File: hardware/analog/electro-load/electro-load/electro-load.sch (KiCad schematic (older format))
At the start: 10 parts

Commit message: Added datasheets for noctua fan, mcu and lm358 etc.
Finished schematic rev 1 of electro load
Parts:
- removed J? (x2): Conn_01x01_Female, symbol Connector:Conn_01x01_Female
- removed R?: R_Small, symbol Device:R_Small
- removed RV?: R_POT, symbol Device:R_POT
- removed U?: OPAMP, symbol pspice:OPAMP
- removed U?: ATMEGA328P-AU, digikey-footprints:TQFP-32_7x7mm, symbol dk_Embedded-Microcontrollers:ATMEGA328P-AU
- added C1, C4, C5, C7: 10u, Capacitor_SMD:C_0603_1608Metric, symbol Device:C_Small
- added C2, C3, C6: 100n, Capacitor_SMD:C_0603_1608Metric, symbol Device:C_Small
- added D1: STATUS, LED_THT:LED_D5.0mm-4_RGB_Wide_Pins, symbol Device:LED_ABRG
- added D3: D_Schottky, athir:SOD80C(Reflow), symbol Device:D_Schottky
- added J1: Barrel_Jack, athir:6778759, symbol Connector:Barrel_Jack
- added J3: AVR-ISP-10, Connector_PinHeader_2.54mm:PinHeader_2x05_P2.54mm_Vertical, symbol Connector:AVR-ISP-10
- added K1: SANYOU_SRD_Form_C, Relay_THT:Relay_SPDT_SANYOU_SRD_Series_Form_C, symbol Relay:SANYOU_SRD_Form_C
- added M1: Noctua NF-A14 5V, Connector_PinHeader_2.54mm:PinHeader_1x04_P2.54mm_Vertical, symbol Motor:Fan_4pin
- added Q2, Q4: 2N2222A, Package_TO_SOT_THT:TO-92_Inline, symbol dk_Transistors-Bipolar-BJT-Single:2N2222A
- added Q3: 2N2222, Package_TO_SOT_THT:TO-92_Inline, symbol dk_Transistors-Bipolar-BJT-Single:2N2222
- added R1: 2k, Resistor_SMD:R_0603_1608Metric, symbol Device:R_Small
- added R11: 825k, Resistor_SMD:R_0603_1608Metric, symbol Device:R_Small
- added R13: 2ohm 128++W, Connector_PinSocket_2.54mm:PinSocket_1x02_P2.54mm_Vertical, symbol Device:R_Small
- added R14, R15, R20, R21: 10k POT, Potentiometer_SMD:Potentiometer_Bourns_3214W_Vertical, symbol Device:R_Small
- added R16, R17, R22, R23, R24, R28, R29, R30: 1k, Resistor_SMD:R_0603_1608Metric, symbol Device:R_Small
- added R18, R4, R5: 4k7, Resistor_SMD:R_0603_1608Metric, symbol Device:R_Small
- added R19, R25: 3k3, Resistor_SMD:R_0603_1608Metric, symbol Device:R_Small
- added R2: 220, Resistor_SMD:R_0603_1608Metric, symbol Device:R_Small
- added R26, R27, R3: 10k, Resistor_SMD:R_0603_1608Metric, symbol Device:R_Small
- added R6: 200, Resistor_SMD:R_0603_1608Metric, symbol Device:R_Small
- added R8: 10M 1%, Resistor_SMD:R_0603_1608Metric, symbol Device:R_Small
- added R9: 1M5 1%, Resistor_SMD:R_0603_1608Metric, symbol Device:R_Small
- added SW1: RESET, symbol Switch:SW_Push
- added TP1, TP10, TP11, TP12, TP13, TP2, TP3, TP4, TP5, TP6, TP7, TP8, TP9: TestPoint, athir:testpoint_probe, symbol Connector:TestPoint
- added U2: ATmega328P-AU, Package_QFP:TQFP-32_7x7mm_P0.8mm, symbol MCU_Microchip_ATmega:ATmega328P-AU
- added U3: MCP4725A0T-E_CH, digikey-footprints:SOT-23-6, symbol dk_Data-Acquisition-Digital-to-Analog-Converters-DAC:MCP4725A0T-E_CH
- added U4, U5: LM358DR, digikey-footprints:SOIC-8_W3.9mm, symbol dk_Linear-Amplifiers-Instrumentation-OP-Amps-Buffer-Amps:LM358DR
- Q1: renamed from Q?; footprint (none) -> Package_TO_SOT_SMD:TO-263-2
- R10: renamed from R?; value R_Small -> 2M; footprint (none) -> Resistor_SMD:R_0603_1608Metric
- R12: renamed from R?; value 2ohm -> 2R 128++W; footprint (none) -> Connector_PinSocket_2.54mm:PinSocket_1x02_P2.54mm_Vertical
- gave numbers to parts that had none: 1
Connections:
- net labels added: CUR_MEAS, CUR_SET, FAN_PWM, FAN_RPM, LCD_DB4, LCD_DB5, LCD_DB6, LCD_DB7, LCD_EN, LCD_RS, LCD_RW, MISO, MOSI, RELAY_EN, SCK, SCL, SDA, STATUS_B, STATUS_G, STATUS_R, TEMP_0, TEMP_1, VCC, V_IN, ~RESET
- wire segments 19 -> 227
- no-connect marks 0 -> 12
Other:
- note added: "DC_OFFSET\nZERO OFFSET"
- note added: "GAIN"
- note added: "OBS: 2N2222A vs -A har forskelligt PINOUT!!"
- moved on the sheet: R10, R12, U1

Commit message: Spread schematic out into multiple subsheets. Removed LEDs as pins was needed for 16x2 display
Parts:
- removed D1: STATUS, LED_THT:LED_D5.0mm-4_RGB_Wide_Pins, symbol Device:LED_ABRG
- removed D3: D_Schottky, athir:SOD80C(Reflow), symbol Device:D_Schottky
- removed J1: Barrel_Jack, athir:6778759, symbol Connector:Barrel_Jack
- removed K1: SANYOU_SRD_Form_C, Relay_THT:Relay_SPDT_SANYOU_SRD_Series_Form_C, symbol Relay:SANYOU_SRD_Form_C
- removed M1: Noctua NF-A14 5V, Connector_PinHeader_2.54mm:PinHeader_1x04_P2.54mm_Vertical, symbol Motor:Fan_4pin
- removed Q1: Q_NJFET_GDS, Package_TO_SOT_SMD:TO-263-2, symbol Device:Q_NJFET_GDS
- removed Q2, Q4: 2N2222A, Package_TO_SOT_THT:TO-92_Inline, symbol dk_Transistors-Bipolar-BJT-Single:2N2222A
- removed Q3: 2N2222, Package_TO_SOT_THT:TO-92_Inline, symbol dk_Transistors-Bipolar-BJT-Single:2N2222
- removed R1: 2k, Resistor_SMD:R_0603_1608Metric, symbol Device:R_Small
- removed R10: 2M, Resistor_SMD:R_0603_1608Metric, symbol Device:R_Small
- removed R11: 825k, Resistor_SMD:R_0603_1608Metric, symbol Device:R_Small
- removed R12: 2R 128++W, Connector_PinSocket_2.54mm:PinSocket_1x02_P2.54mm_Vertical, symbol Device:R_Small
- removed R13: 2ohm 128++W, Connector_PinSocket_2.54mm:PinSocket_1x02_P2.54mm_Vertical, symbol Device:R_Small
- removed R14, R15, R20, R21: 10k POT, Potentiometer_SMD:Potentiometer_Bourns_3214W_Vertical, symbol Device:R_Small
- removed R16, R17, R22, R23, R24, R28, R29, R30: 1k, Resistor_SMD:R_0603_1608Metric, symbol Device:R_Small
- removed R18: 4k7, Resistor_SMD:R_0603_1608Metric, symbol Device:R_Small
- removed R19, R25: 3k3, Resistor_SMD:R_0603_1608Metric, symbol Device:R_Small
- removed R2: 220, Resistor_SMD:R_0603_1608Metric, symbol Device:R_Small
- removed R26, R27: 10k, Resistor_SMD:R_0603_1608Metric, symbol Device:R_Small
- removed R6: 200, Resistor_SMD:R_0603_1608Metric, symbol Device:R_Small
- removed R8: 10M 1%, Resistor_SMD:R_0603_1608Metric, symbol Device:R_Small
- removed R9: 1M5 1%, Resistor_SMD:R_0603_1608Metric, symbol Device:R_Small
- removed TP10, TP11, TP12, TP13, TP4, TP5, TP6, TP7, TP8, TP9: TestPoint, athir:testpoint_probe, symbol Connector:TestPoint
- removed U1: RC1602A, Displays:RC1602A, symbol athir:RC1602A
- removed U4, U5: LM358DR, digikey-footprints:SOIC-8_W3.9mm, symbol dk_Linear-Amplifiers-Instrumentation-OP-Amps-Buffer-Amps:LM358DR
- renumbered J3 to J1, R3 to R1, R4 to R2, R5 to R3, U2 to U1, U3 to U2
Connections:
- net labels removed: VCC, V_IN
- wire segments 227 -> 65
- no-connect marks 12 -> 3
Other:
- note removed: "DC_OFFSET\nZERO OFFSET"
- note removed: "GAIN"
- note removed: "OBS: 2N2222A vs -A har forskelligt PINOUT!!"

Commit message: HW rev 1 of electronic load PCB.
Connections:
- net LCD_DB5: now also U1.11 (PD7); no longer U1.9 (PD5)
- net LCD_DB7: now also U1.9 (PD5); no longer U1.11 (PD7)
- net V_MEAS: now reaches U1.24 (PC1)
- net STATUS_B renamed ROT_SW
- net STATUS_G renamed ROT_B
- net STATUS_R renamed ROT_A
- no-connect marks 3 -> 2
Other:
- note added: "OBS"
- moved on the sheet: J1
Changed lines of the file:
@@
 EESchema Schematic File Version 4
-LIBS:electro-load-cache
 EELAYER 30 0
 EELAYER END
@@
 Wire Wire Line
 	2000 7025 2000 6975
-Text Label 2600 4875 0    50   ~ 0
-STATUS_R
-Text Label 2600 4975 0    50   ~ 0
-STATUS_G
-Text Label 2600 5975 0    50   ~ 0
-STATUS_B
-Wire Wire Line
-	2875 5175 2600 5175
 Text Label 2600 4475 0    50   ~ 0
 RELAY_EN
@@
 Text Label 2600 5375 0    50   ~ 0
 TEMP_1
-Text Label 2875 5175 0    50   ~ 0
+Text Label 2600 5175 0    50   ~ 0
 CUR_MEAS
 Text Label 4425 1875 0    50   ~ 0
@@
 Wire Wire Line
 	2600 4000 2400 4000
-Text Label 10975 5675 0    50   ~ 0
+Text Label 8750 5500 0    50   ~ 0
 MOSI
-Text Label 10975 5875 0    50   ~ 0
+Text Label 8750 5700 0    50   ~ 0
 ~RESET
-Text Label 10975 5775 0    50   ~ 0
+Text Label 8750 5600 0    50   ~ 0
 SCK
-Text Label 10975 5575 0    50   ~ 0
+Text Label 8750 5400 0    50   ~ 0
 MISO
 $Comp
 L power:+5V #PWR012
 U 1 1 5E81DCEE
-P 10475 5225
-F 0 "#PWR012" H 10475 5075 50  0001 C CNN
-F 1 "+5V" H 10490 5398 50  0000 C CNN
-F 2 "" H 10475 5225 50  0001 C CNN
-F 3 "" H 10475 5225 50  0001 C CNN
-	1    10475 5225
+P 8250 5050
+F 0 "#PWR012" H 8250 4900 50  0001 C CNN
+F 1 "+5V" H 8265 5223 50  0000 C CNN
+F 2 "" H 8250 5050 50  0001 C CNN
+F 3 "" H 8250 5050 50  0001 C CNN
+	1    8250 5050
 	1    0    0    -1
 $EndComp
@@
 L power:GND #PWR013
 U 1 1 5E8275B7
-P 10475 6250
-F 0 "#PWR013" H 10475 6000 50  0001 C CNN
-F 1 "GND" H 10480 6077 50  0000 C CNN
-F 2 "" H 10475 6250 50  0001 C CNN
-F 3 "" H 10475 6250 50  0001 C CNN
-	1    10475 6250
+P 8250 6075
+F 0 "#PWR013" H 8250 5825 50  0001 C CNN
+F 1 "GND" H 8255 5902 50  0000 C CNN
+F 2 "" H 8250 6075 50  0001 C CNN
+F 3 "" H 8250 6075 50  0001 C CNN
+	1    8250 6075
 	1    0    0    -1
 $EndComp
@@
 L Connector:AVR-ISP-10 J1
 U 1 1 5E855F65
-P 10575 5775
-F 0 "J1" H 10295 5871 50  0000 R CNN
-F 1 "AVR-ISP-10" H 10295 5780 50  0000 R CNN
-F 2 "Connector_PinHeader_2.54mm:PinHeader_2x05_P2.54mm_Vertical" V 10325 5825 50  0001 C CNN
-F 3 " ~" H 9300 5225 50  0001 C CNN
-	1    10575 5775
-	1    0    0    -1
-$EndComp
-Wire Wire Line
-	10475 6250 10475 6175
-Wire Wire Line
-	10475 5225 10475 5275
+P 8350 5600
+F 0 "J1" H 8070 5696 50  0000 R CNN
+F 1 "AVR-ISP-10" H 8070 5605 50  0000 R CNN
+F 2 "Connector_PinHeader_2.54mm:PinHeader_2x05_P2.54mm_Vertical" V 8100 5650 50  0001 C CNN
+F 3 " ~" H 7075 5050 50  0001 C CNN
+	1    8350 5600
+	1    0    0    -1
+$EndComp
+Wire Wire Line
+	8250 6075 8250 6000
+Wire Wire Line
+	8250 5050 8250 5100
 Text Label 2600 4575 0    50   ~ 0
 MOSI
@@
 Connection ~ 3975 1250
 $Sheet
-S 4850 6900 700  525
+S 4650 6100 700  525
 U 5E8D69C1
 F0 "Power" 50
@@
 Text Label 2600 6075 0    50   ~ 0
 LCD_EN
-Text Label 2600 6675 0    50   ~ 0
+Text Label 2600 6475 0    50   ~ 0
 LCD_DB7
 Text Label 2600 6575 0    50   ~ 0
 LCD_DB6
-Text Label 2600 6475 0    50   ~ 0
+Text Label 2600 6675 0    50   ~ 0
 LCD_DB5
 Text Label 2600 6375 0    50   ~ 0
 LCD_DB4
-NoConn ~ 2600 5275
 $Sheet
-S 3825 6800 675  525
+S 5200 4125 1025 200
 U 5E789C0B
 F0 "Temperature Control" 50
 F1 "tempctl.sch" 50
+F2 "TEMP_1" I L 5200 4250 50
+F3 "TEMP_0" I L 5200 4175 50
+F4 "FAN_RPM" I R 6225 4175 50
+F5 "FAN_PWM" I R 6225 4250 50
 $EndSheet
 $Sheet
-S 5725 6425 1050 1000
+S 5300 5000 875  575
 U 5E7EC7EF
 F0 "UI" 50
 F1 "ui.sch" 50
+F2 "LCD_RS" I L 5300 5050 50
+F3 "LCD_RW" I L 5300 5125 50
+F4 "LCD_EN" I L 5300 5200 50
+F5 "LCD_DB4" I L 5300 5275 50
+F6 "LCD_DB5" I L 5300 5350 50
+F7 "LCD_DB6" I L 5300 5425 50
+F8 "LCD_DB7" I L 5300 5500 50
+F9 "ROT_SW" I R 6175 5050 50
+F10 "ROT_A" I R 6175 5125 50
+F11 "ROT_B" I R 6175 5200 50
 $EndSheet
 $Sheet
-S 6850 1950 1675 1625
+S 6850 1950 1075 275
 U 5E82E2D2
 F0 "Current Measurements" 50
 F1 "current.sch" 50
+F2 "V_MEAS" I R 7925 2025 50
+F3 "CUR_MEAS" I L 6850 2025 50
+F4 "CUR_SET" I L 6850 2125 50
+F5 "RELAY_EN" I R 7925 2125 50
 $EndSheet
+Text Label 5300 5050 2    50   ~ 0
+LCD_RS
+Text Label 5300 5125 2    50   ~ 0
+LCD_RW
+Text Label 5300 5200 2    50   ~ 0
+LCD_EN
+Text Label 5300 5500 2    50   ~ 0
+LCD_DB7
+Text Label 5300 5425 2    50   ~ 0
+LCD_DB6
+Text Label 5300 5350 2    50   ~ 0
+LCD_DB5
+Text Label 5300 5275 2    50   ~ 0
+LCD_DB4
+Text Label 5200 4250 2    50   ~ 0
+TEMP_1
+Text Label 5200 4175 2    50   ~ 0
+TEMP_0
+Text Label 6225 4250 0    50   ~ 0
+FAN_PWM
+Text Label 6225 4175 0    50   ~ 0
+FAN_RPM
+Text Label 7925 2125 0    50   ~ 0
+RELAY_EN
+Text Label 6850 2025 2    50   ~ 0
+CUR_MEAS
+Text Label 6850 2125 2    50   ~ 0
+CUR_SET
+Text Label 2600 5275 0    50   ~ 0
+V_MEAS
+Text Label 7925 2025 0    50   ~ 0
+V_MEAS
+Text Label 6175 5050 0    50   ~ 0
+ROT_SW
+Text Label 6175 5125 0    50   ~ 0
+ROT_A
+Text Label 6175 5200 0    50   ~ 0
+ROT_B
+Text Label 2600 5975 0    50   ~ 0
+ROT_SW
+Text Label 2600 4875 0    50   ~ 0
+ROT_A
+Text Label 2600 4975 0    50   ~ 0
+ROT_B
+Text Notes 3050 6525 0    50   ~ 0
+OBS
 $EndSCHEMATC

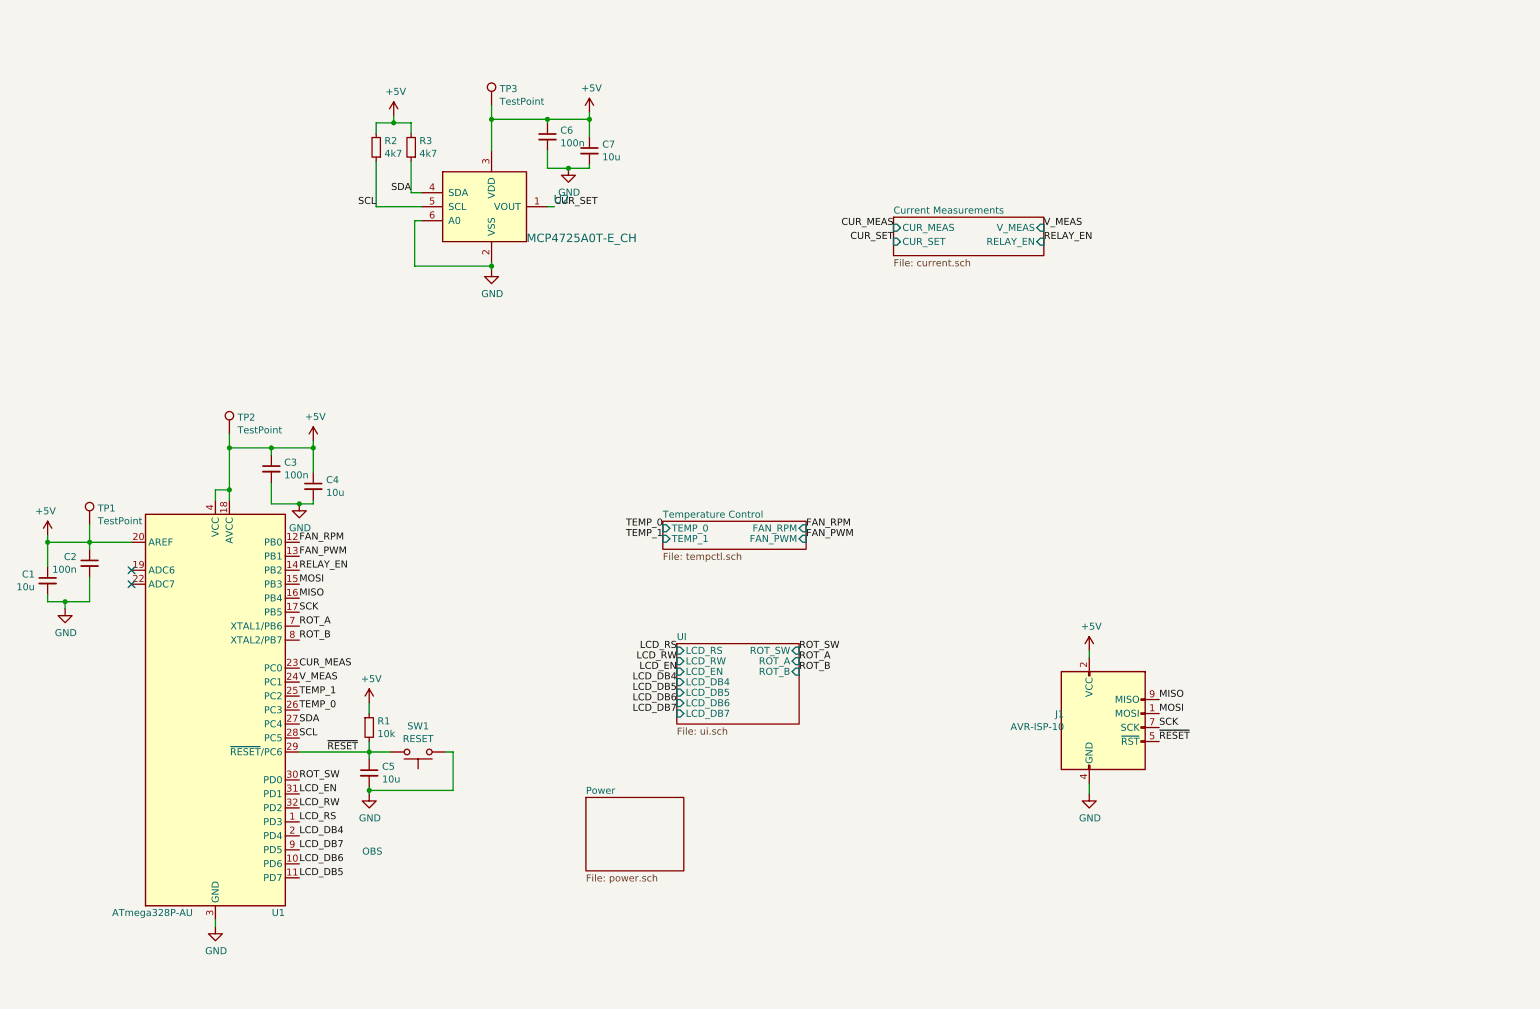
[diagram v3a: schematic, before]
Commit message: Added voltage reference REF5020 datasheet
Started work on HW rev 2 of electro load and 5v-from-mains - rev 1 contained misaligned footprints.
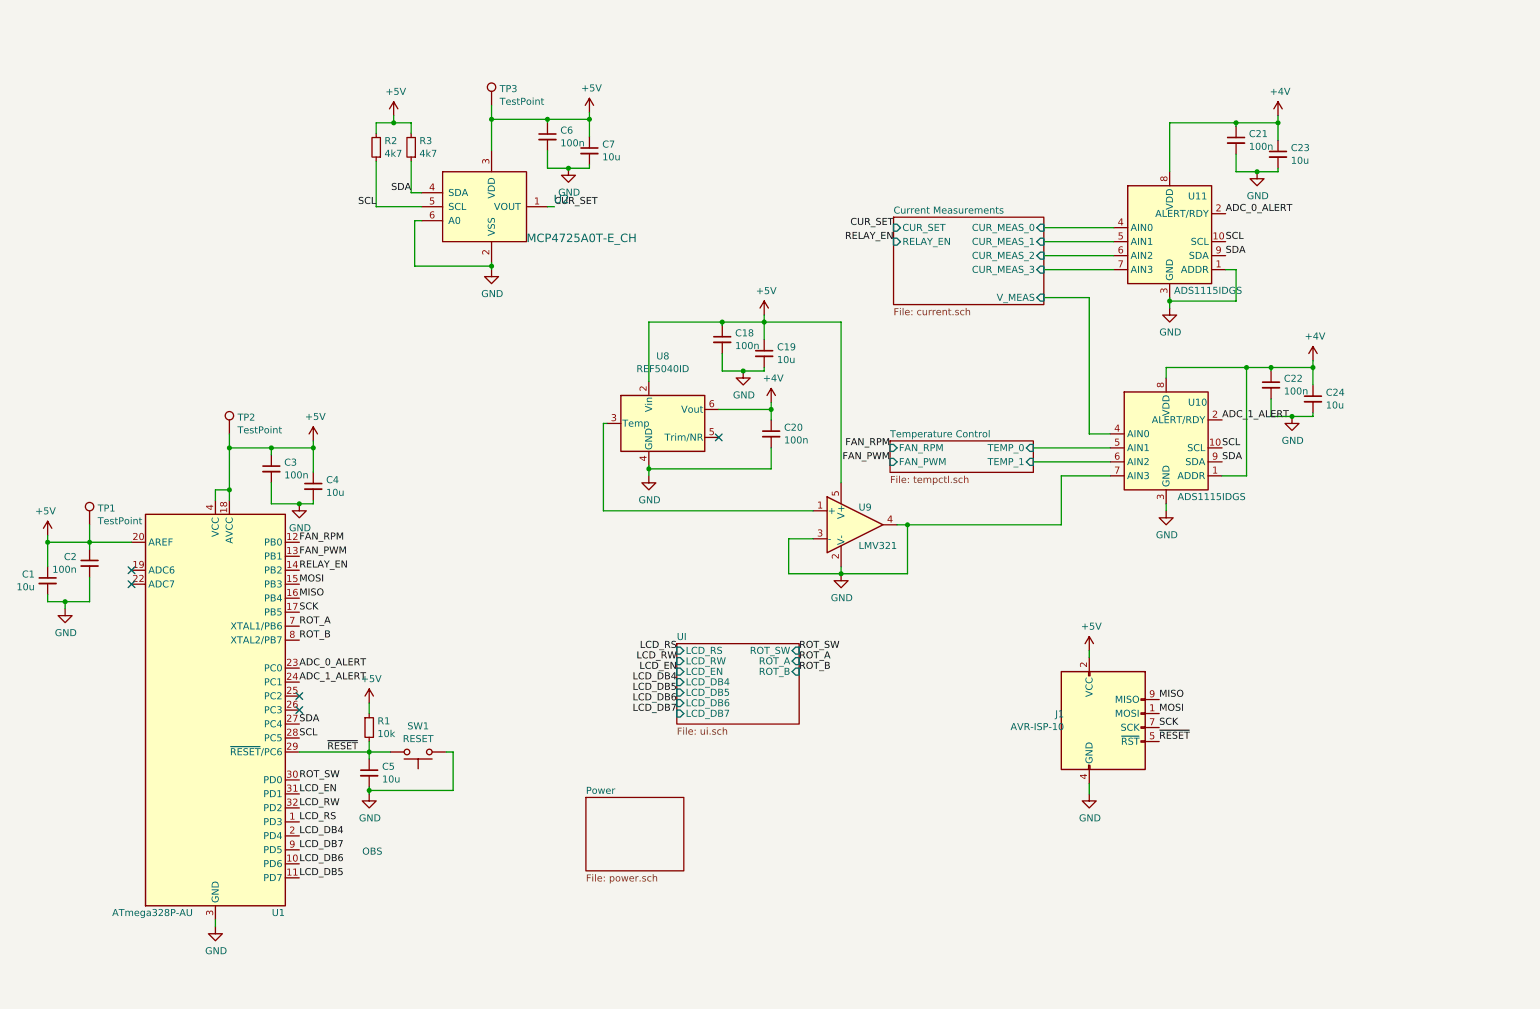
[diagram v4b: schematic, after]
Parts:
- added C18, C20, C21, C22: 100n, Capacitor_SMD:C_0603_1608Metric, symbol Device:C_Small
- added C19, C23, C24: 10u, Capacitor_SMD:C_0603_1608Metric, symbol Device:C_Small
- added U10, U11: ADS1115IDGS, Package_SO:TSSOP-10_3x3mm_P0.5mm, symbol Analog_ADC:ADS1115IDGS
- added U8: REF5040ID, Package_SO:SOIC-8_3.9x4.9mm_P1.27mm, symbol Reference_Voltage:REF5040ID
- added U9: LMV321, Package_TO_SOT_SMD:SOT-23-5, symbol Amplifier_Operational:LMV321
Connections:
- net +5V: now also C18.1, C19.1, U8.2 (Vin), U9.5 (V+)
- net GND: now also C18.2, C19.2, C20.2, C21.2, C22.2, C23.2, C24.2, U10.3 (GND), U10.7 (AIN3), U11.1 (ADDR), U11.3 (GND), U8.4 (GND), U9.2 (V-), U9.3 (-), U9.4
- net SCL: now also U10.10 (SCL), U11.10 (SCL)
- net SDA: now also U10.9 (SDA), U11.9 (SDA)
- net CUR_MEAS renamed ADC_0_ALERT
- net ADC_0_ALERT: now also U11.2 (ALERT/RDY)
- net TEMP_0: no longer names the net of U1.26 (PC3)
- net TEMP_1: no longer names the net of U1.25 (PC2)
- net V_MEAS renamed ADC_1_ALERT
- net ADC_1_ALERT: now also U10.2 (ALERT/RDY)
- new net: U8.3 (Temp), U9.1 (+)
- new net +4V: C20.1, C21.1, C22.1, C23.1, C24.1, U10.1 (ADDR), U10.8 (VDD), U11.8 (VDD), U8.6 (Vout)
- new net Current Measurements/CUR_MEAS_0: U11.4 (AIN0)
- new net Current Measurements/CUR_MEAS_1: U11.5 (AIN1)
- new net Current Measurements/CUR_MEAS_2: U11.6 (AIN2)
- new net Current Measurements/CUR_MEAS_3: U11.7 (AIN3)
- new net Current Measurements/V_MEAS: U10.4 (AIN0)
- new net Temperature Control/TEMP_0: U10.5 (AIN1)
- new net Temperature Control/TEMP_1: U10.6 (AIN2)
- no-connect marks 2 -> 5

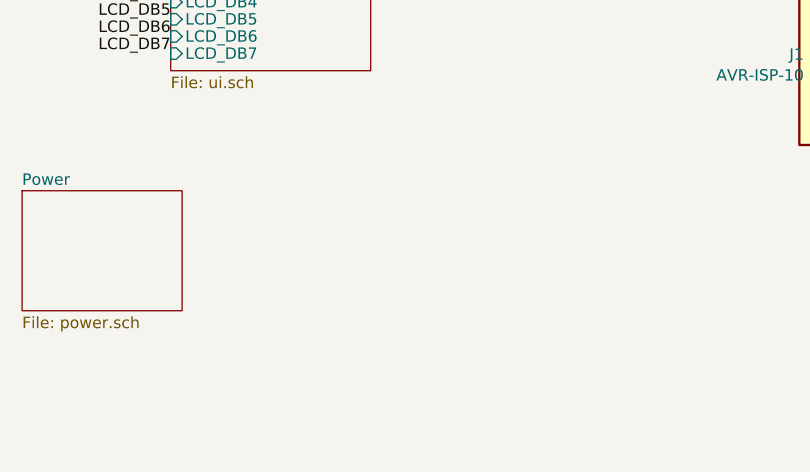
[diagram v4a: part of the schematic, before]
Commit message: Arranged mosfets and temperature probes to amplifier casing.
Added Power schematic from 5v-from-mains
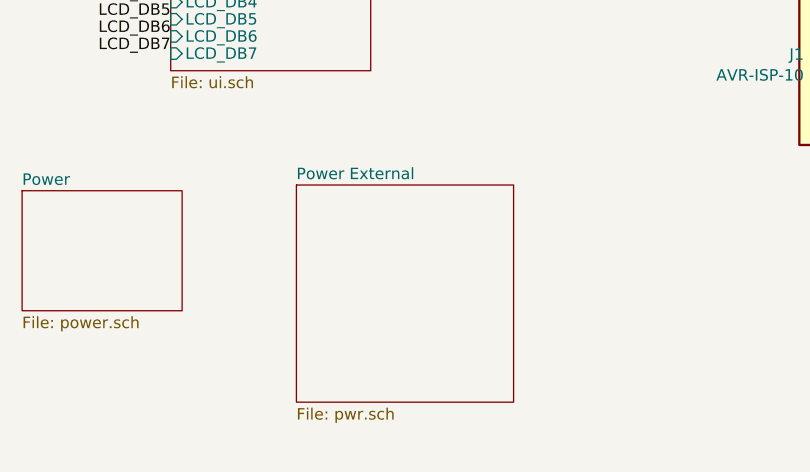
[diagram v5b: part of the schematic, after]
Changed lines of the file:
@@
 EESchema Schematic File Version 4
+LIBS:electro-load-cache
 EELAYER 30 0
 EELAYER END
 $Descr A4 11693 8268
 encoding utf-8
-Sheet 1 5
+Sheet 1 6
 Title ""
 Date ""
@@
 NoConn ~ 2600 5375
 NoConn ~ 2600 5475
+$Sheet
+S 5850 6075 950  950
+U 5E9F0954
+F0 "Power External" 50
+F1 "pwr.sch" 50
+$EndSheet
 $EndSCHEMATC
